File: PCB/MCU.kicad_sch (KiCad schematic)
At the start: 25 parts, among them U1 STM32G431CBT6, Y1 8MHz

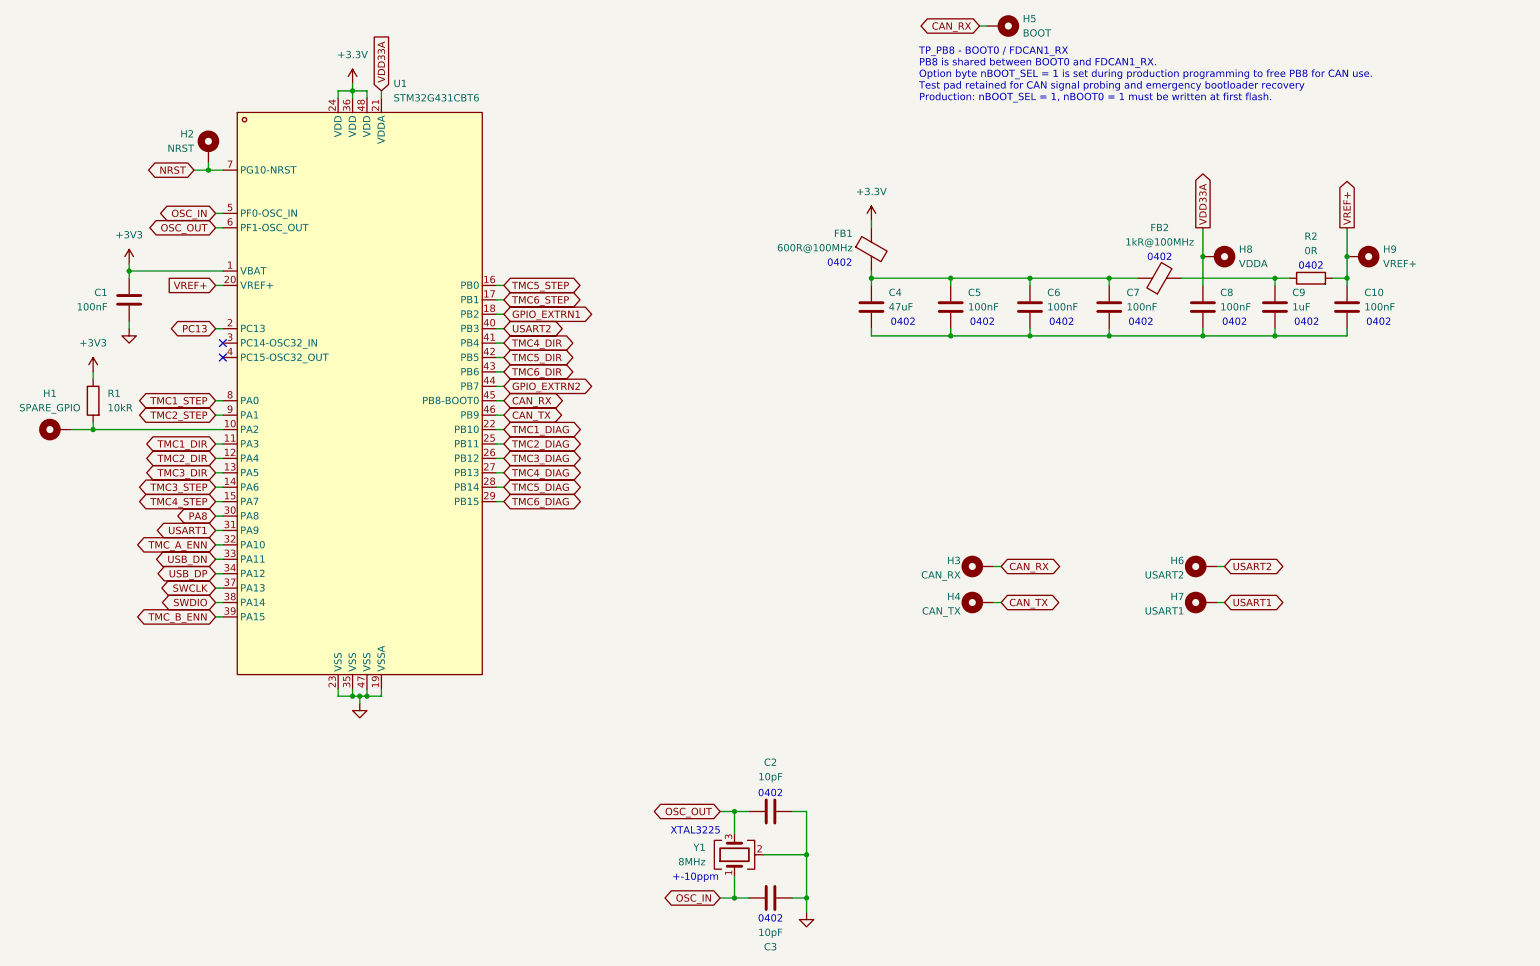
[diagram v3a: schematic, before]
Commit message: Continued PCB Development - Routed MCU decoupeling and Isolated Crystal - Routed LDO Buck converter (VBUS (+5V) -> +3V3) - Routed Buck Converter (+24V -> +3V3) needs review (U2-pin1-GND) - Started Routing TMC2209 to their terminal blocks - Noticed issue with Stepper Lines coupeling back into +24V - TODO: Move Motor Input farther inside and add grounding isolation - Fixed Polariy mismatch with J3 (XT60 Battery Connector)
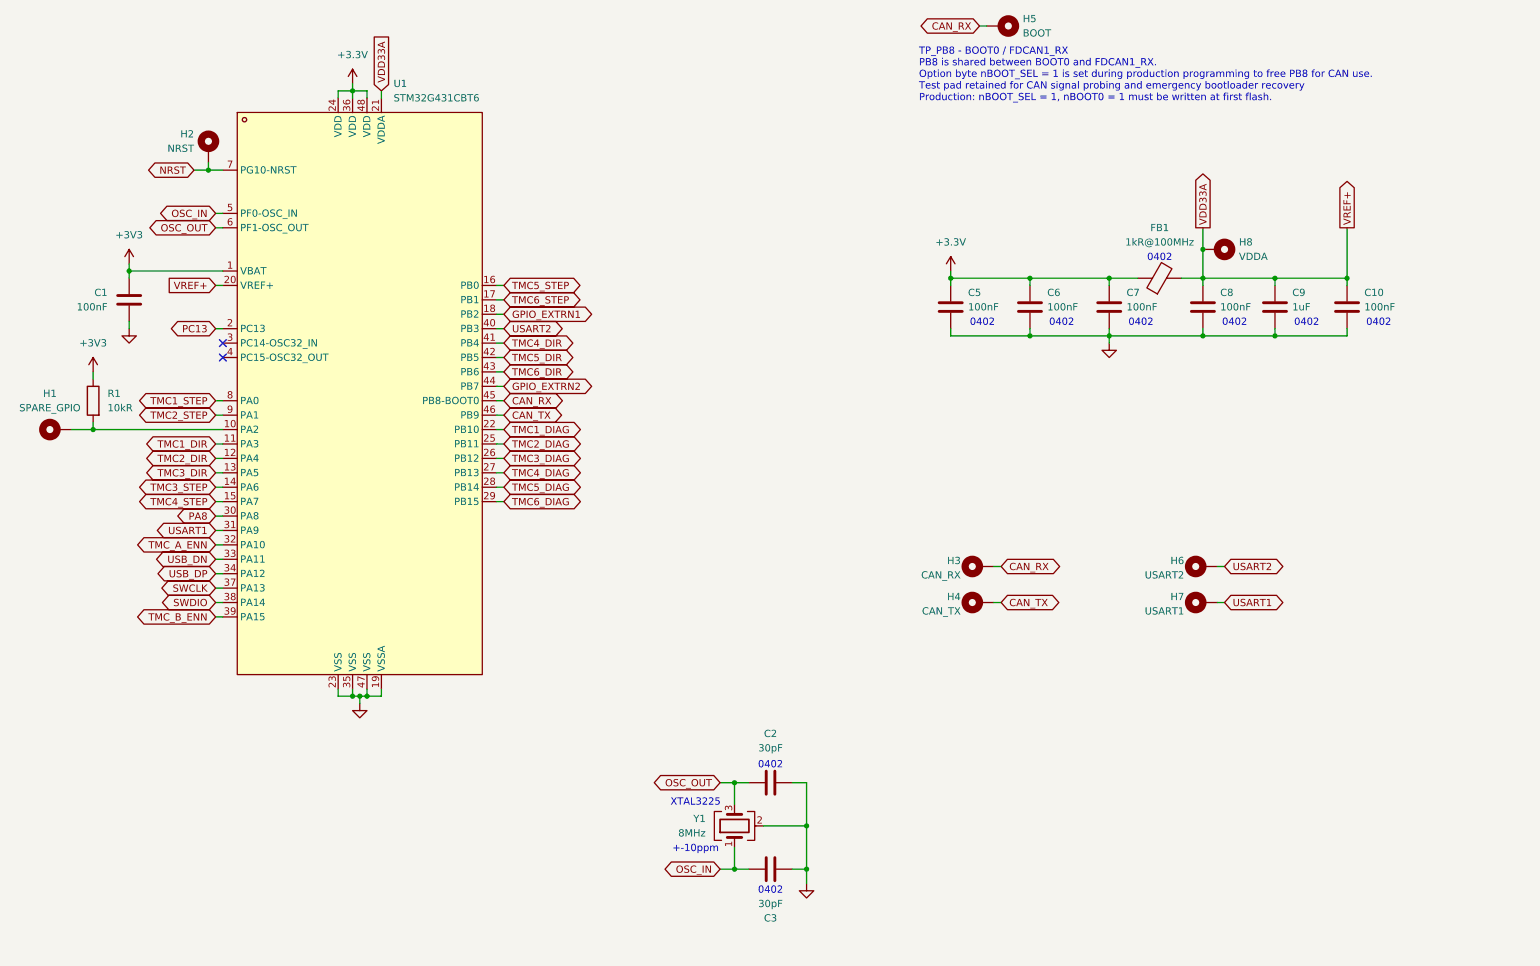
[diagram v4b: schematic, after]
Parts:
- removed C4: 47uF, Capacitor_SMD:C_0603_1608Metric, symbol Device:C
- removed FB1: 600R@100MHz, Inductor_SMD:L_0402_1005Metric, symbol Device:FerriteBead
- removed H9: VREF+, TestPoint:TestPoint_Pad_D2.0mm, symbol Mechanical:MountingHole_Pad
- removed R2: 0R, Resistor_SMD:R_0402_1005Metric, symbol Device:R
- C2, C3: value 10pF -> 30pF
- renumbered FB2 to FB1
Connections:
- net VREF+ is gone; now on net VDD33A: C10.1, U1.20 (VREF+)
- net +3.3V: now also C5.1, C6.1, C7.1, FB1.1
- net GND: now also C10.2, C5.2, C6.2, C7.2, C8.2, C9.2
- net VDD33A: now also C9.1, FB1.2
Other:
- moved on the sheet: C2, C3, H8, Y1
